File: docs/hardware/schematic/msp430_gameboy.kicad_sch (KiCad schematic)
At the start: 27 parts, among them J1 OLED_SPI, J2 LiPo_Charger, SW1 SW_BTN_A, SW2 SW_BTN_B, SW3 SW_BTN_C, SW4 SW_BTN_D, SW5 SW_BTN_E, SW6 SW_BTN_F, SW7 SW_BTN_G, SW8 SW_BTN_H, U1 MSP430G2553, U2 SN74HC165N, U3 LM386N-1

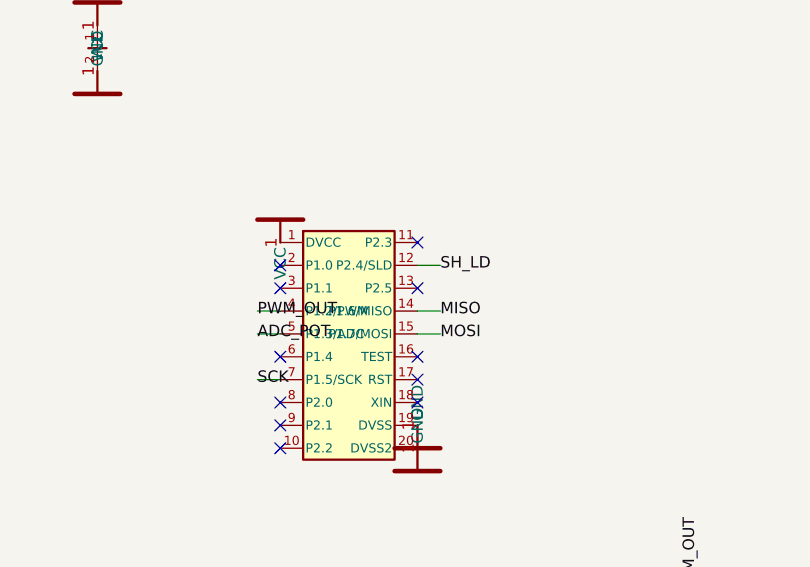
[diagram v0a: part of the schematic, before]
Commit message: fix: hardware docs Rev B — correct SPI pins, display, add memory ICs
breadboard_guide.md (Rev B): full rewrite — fix OLED DFR0650→SSD1325 SPI,
fix SR QH→P1.6 (was P1.7), fix SH/LD→P2.5 (was P2.4), add SRAM and
Flash wiring tables, remove ADC pot, update LaunchPad rows to match
photo (~rows 20-40), correct LM386 pinout, add SPI CS management note.

breadboard_layout.html: move LaunchPad to rows 20-40, add SRAM/Flash
components, replace DFR0650→SSD1325 SPI, remove ADC pot, fix J2 pin
labels (P2.3=SRAM_CS, P2.4=Flash_CS, P2.5=SH/LD), fix legend.

phase-2-oled-display.md: SSD1309→SSD1325, add SRAM+Flash sections,
explain why external SRAM is needed (4096-byte framebuffer).

msp430_gameboy.kicad_sch: fix title block SPI comments, rename MCU
pins P2.4→FCSN and P2.5→SLD, move SH_LD net to P2.5, add FLASH_CS
at P2.4 and SRAM_CS at P2.3.

Co-Authored-By: Claude Sonnet 4.6 <noreply@anthropic.com>
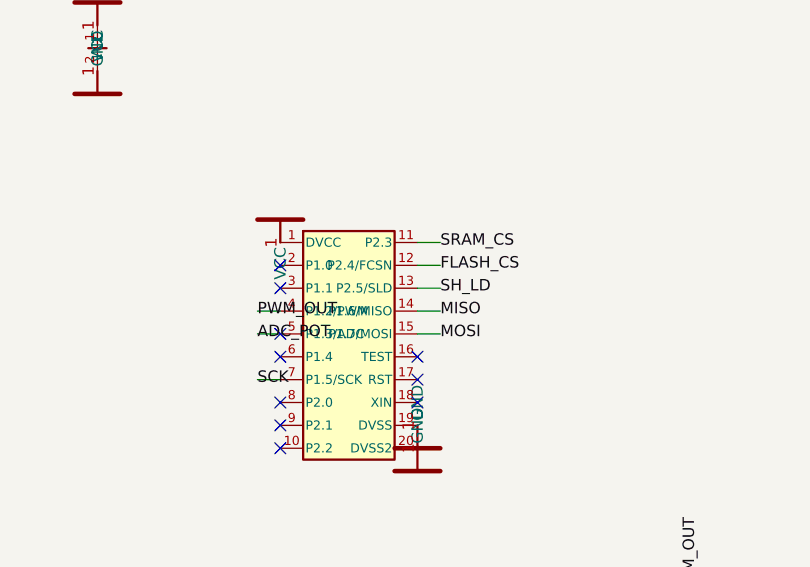
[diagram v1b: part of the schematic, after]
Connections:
- net SH_LD: now also U1.13 (P2.5/SLD); no longer U1.12 (P2.4/SLD)
- net SRAM_CS: now reaches U1.11 (P2.3)
- new net FLASH_CS: U1.12 (P2.4/FCSN)
- no-connect marks 17 -> 16
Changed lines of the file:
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@@
     (company "")
     (comment 1 "MCU: MSP430G2553 (LaunchPad MSP-EXP430G2)")
-    (comment 2 "SPI: P1.5=SCK  P1.6=MISO  P1.7=MOSI  P2.4=SH/LD#")
-    (comment 3 "Audio: P1.2-PWM -> 1k+100nF -> LM386N-IN- -> OUTPUT -> 8ohm speaker")
-    (comment 4 "Buttons: SN74HC165N parallel-in/serial-out, 10k pull-ups, BTN_A..H")
+    (comment 2 "SPI bus (USCI_B0): P1.5=SCK  P1.6=MISO  P1.7=MOSI")
+    (comment 3 "CS: P2.0=OLED_CS  P2.1=OLED_DC  P2.2=OLED_RST  P2.3=SRAM_CS  P2.4=Flash_CS  P2.5=SH/LD#")
+    (comment 4 "Devices: SSD1325 OLED | 23LC1024 SRAM (128KB) | W25Q128JVSSIQ Flash (16MB, Adafruit #5634) | SN74HC165N buttons")
   )
   (symbol (lib_id "MSP430G2553") (at 175.2600 124.4600 0) (unit 1) (exclude_from_sim no) (in_bom yes) (on_board yes) (dnp no) (property "Reference" "U1"  (at 175.2600 124.4600 0) (effects (font (size 1.27 1.27)) (hide))) (property "Value" "MSP430G2553"  (at 175.2600 124.4600 0) (effects (font (size 1.27 1.27)) (hide))))
@@
   (label "ADC_POT" (at 165.1000 123.1900 180) (fields_autoplaced yes) (effects (font (size 1.27 1.27)) (justify left)))
   (label "SCK" (at 165.1000 128.2700 180) (fields_autoplaced yes) (effects (font (size 1.27 1.27)) (justify left)))
-  (label "SH_LD" (at 185.4200 115.5700 0) (fields_autoplaced yes) (effects (font (size 1.27 1.27)) (justify left)))
+  (label "FLASH_CS" (at 185.4200 115.5700 0) (fields_autoplaced yes) (effects (font (size 1.27 1.27)) (justify left)))
+  (wire (pts (xy 182.8800 118.1100) (xy 185.4200 118.1100)) (stroke (width 0) (type default)))
+  (label "SH_LD" (at 185.4200 118.1100 0) (fields_autoplaced yes) (effects (font (size 1.27 1.27)) (justify left)))
+  (wire (pts (xy 182.8800 113.0300) (xy 185.4200 113.0300)) (stroke (width 0) (type default)))
+  (label "SRAM_CS" (at 185.4200 113.0300 0) (fields_autoplaced yes) (effects (font (size 1.27 1.27)) (justify left)))
   (label "MISO" (at 185.4200 120.6500 0) (fields_autoplaced yes) (effects (font (size 1.27 1.27)) (justify left)))
   (label "MOSI" (at 185.4200 123.1900 0) (fields_autoplaced yes) (effects (font (size 1.27 1.27)) (justify left)))
@@
   (no_connect (at 167.6400 133.3500))
   (no_connect (at 167.6400 135.8900))
-  (no_connect (at 182.8800 113.0300))
-  (no_connect (at 182.8800 118.1100))
+  (no_connect (at 167.6400 123.1900))
   (no_connect (at 182.8800 125.7300))
   (no_connect (at 182.8800 128.2700))
